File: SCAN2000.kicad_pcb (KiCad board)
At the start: 2 copper layers, 228.6 x 70.6 mm, 132 parts, among them J1 Conn_02x16_Row_Letter_First, J2 Conn_01x05, J3 Conn_01x02, J4 Screw_Terminal_01x02, J5 Screw_Terminal_01x10, J6 Screw_Terminal_01x10, J7 Screw_Terminal_01x02, J8 Screw_Terminal_01x10, J9 Screw_Terminal_01x10, U1 TPS73233DBVR, U10 TLP3558A, U11 TLP3558A, U12 TLP3558A, U13 TLP3558A, U14 TLP3558A, U15 TLP3558A, U16 TLP3558A, U17 TLP3558A, U18 TLP3558A, U19 TLP3558A, U20 TLP3558A, U21 TLP3558A, U22 TLP3558A, U23 TLP3558A, U24 TLP3558A, U25 TLP3558A, U26 TLP3558A, U27 TLP3558A, U28 TLP3558A, U29 TLP3558A, U3 STM32G070KBT6, U30 TLP3558A, U31 TLP3558A, U32 TLP3558A, U33 TLP3558A, U34 TLP3558A, U35 TLP3558A, U36 TLP3558A, U37 TLP3558A, U38 TLP3558A, U39 TLP3558A, U4 TLP3558A, U40 TLP3558A, U41 TLP3558A, U42 TLP3558A, U43 TLP3558A, U44 TLP3558A, U45 TLP3558A, U46 TLP3558A, U47 TLP3558A, U5 TLP3558A, U6 TLP3558A, U7 TLP3558A, U8 TLP3558A, U9 TLP3558A

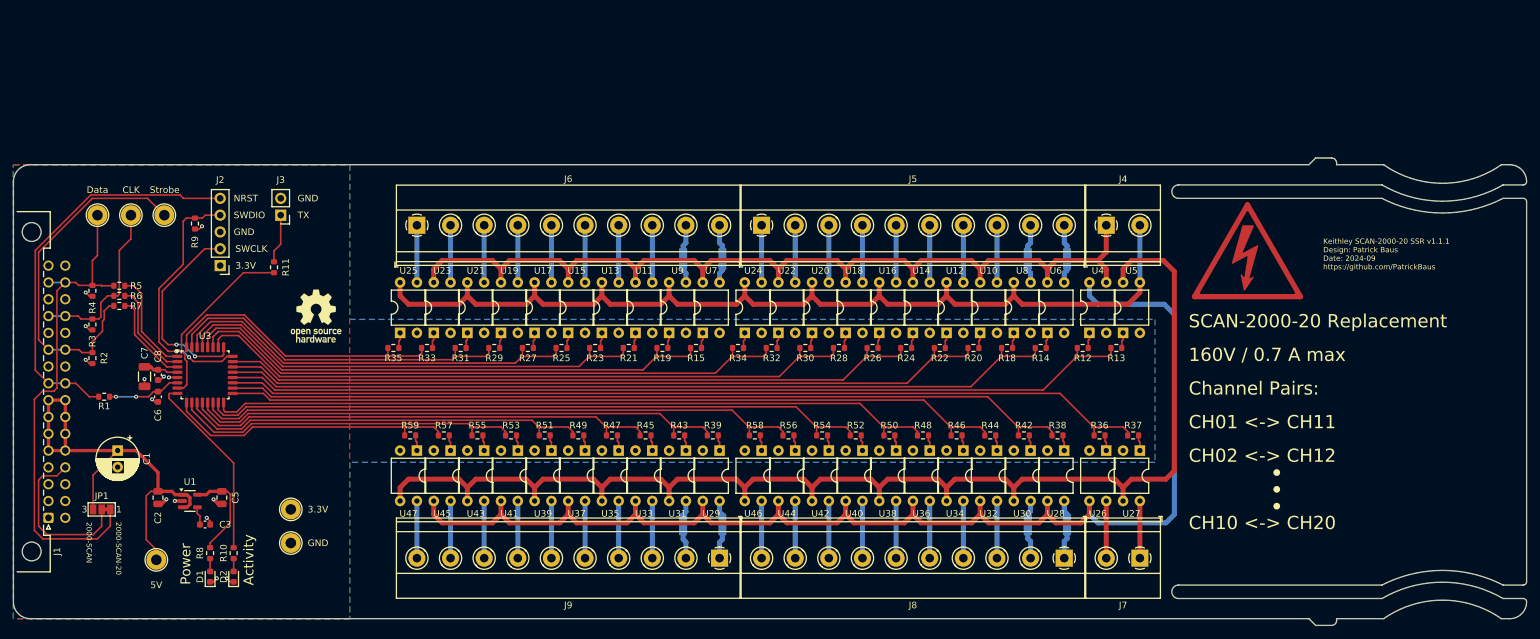
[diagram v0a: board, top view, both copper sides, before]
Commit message: Replaced the STM32 microcontroller with an iCE40 FPGA
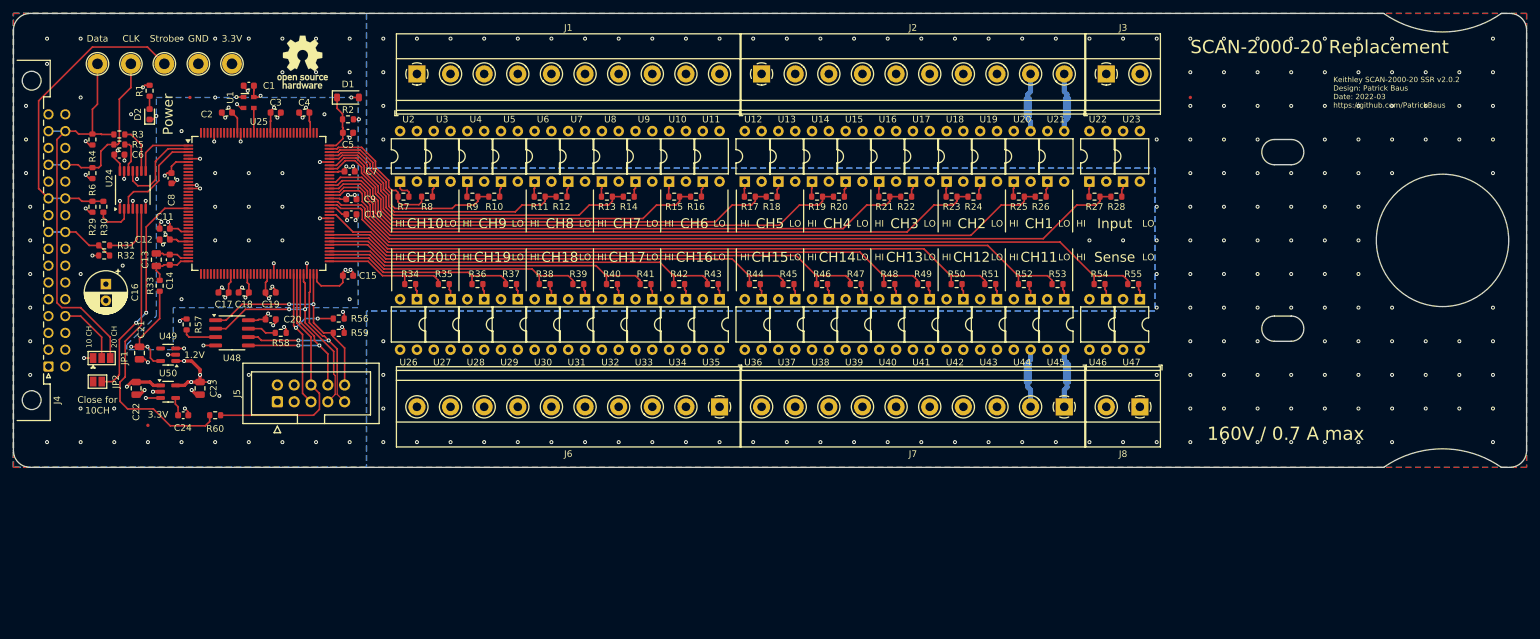
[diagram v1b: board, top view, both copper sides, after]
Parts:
- removed the D2 at (58.7, 110.5)
- removed the J2 at (56.6, 63.5)
- removed the J3 at (65.8, 55.9)
- removed the R10 at (58.7, 106.9)
- removed the R11 at (64.8, 63.8)
- removed the R17 at (129.5, 62.5)
- removed the R41 at (129.5, 102.6)
- removed the R9 at (52.8, 57.1)
- removed SYM1: SYM_Flash_Small, Symbol:Symbol_HighVoltage_Triangle_17x15mm_Copper
- removed the TP1 at (47.0, 108.0)
- removed the U3 at (54.4, 80.0)
- added C1: 100n, Capacitor_SMD:C_0603_1608Metric, F.Cu at (61.0, 36.3)
- added C10: 100n, Capacitor_SMD:C_0603_1608Metric, F.Cu at (76.5, 55.8)
- added C11: 100n, Capacitor_SMD:C_0603_1608Metric, F.Cu at (48.3, 57.9)
- added C12: 100n, Capacitor_SMD:C_0603_1608Metric, F.Cu at (48.3, 59.6)
- added C13: 10u, Capacitor_SMD:C_0805_2012Metric, F.Cu at (47.0, 62.6)
- added C14: 100n, Capacitor_SMD:C_0603_1608Metric, F.Cu at (49.0, 62.6)
- added C17: 100n, Capacitor_SMD:C_0603_1608Metric, F.Cu at (57.1, 67.6)
- added C18: 100n, Capacitor_SMD:C_0603_1608Metric, F.Cu at (60.2, 67.6)
- added C19: 100n, Capacitor_SMD:C_0603_1608Metric, F.Cu at (64.3, 67.6)
- added C2: 100n, Capacitor_SMD:C_0603_1608Metric, F.Cu at (57.7, 40.4)
- added C20: 100n, Capacitor_SMD:C_0603_1608Metric, F.Cu at (64.3, 71.6)
- added C21: 1u, Capacitor_SMD:C_0805_2012Metric, F.Cu at (44.5, 76.7)
- added C3: 100n, Capacitor_SMD:C_0603_1608Metric, F.Cu at (65.0, 40.4)
- added C4: 100n, Capacitor_SMD:C_0603_1608Metric, F.Cu at (69.3, 40.4)
- added C5: 100n, Capacitor_SMD:C_0603_1608Metric, F.Cu at (75.9, 43.4)
- added C8: 100n, Capacitor_SMD:C_0603_1608Metric, F.Cu at (49.3, 50.3)
- added C9: 100n, Capacitor_SMD:C_0603_1608Metric, F.Cu at (76.5, 53.5)
- added D1: 1N4448WQ-7-F, Diode_SMD:D_SOD-123, F.Cu at (75.9, 38.1)
- added FID1: Fiducial, Fiducial:Fiducial_0.5mm_Mask1mm, F.Cu at (52.1, 38.1)
- added FID2: Fiducial, Fiducial:Fiducial_0.5mm_Mask1mm, F.Cu at (203.2, 38.1)
- added FID3: Fiducial, Fiducial:Fiducial_0.5mm_Mask1mm, F.Cu at (45.7, 87.6)
- added J5: Conn_02x05_Odd_Even, Connector_IDC:IDC-Header_2x05_P2.54mm_Vertical, F.Cu at (65.3, 84.1)
- added JP2: SolderJumper_2_Open, Jumper:SolderJumper-2_P1.3mm_Open_Pad1.0x1.5mm, F.Cu at (38.1, 81.0)
- added R2: 33k, Resistor_SMD:R_0603_1608Metric, F.Cu at (75.9, 41.4)
- added R32: 10k, Resistor_SMD:R_0603_1608Metric, F.Cu at (39.1, 62.0)
- added R33: 100R, Resistor_SMD:R_0603_1608Metric, F.Cu at (47.5, 66.5)
- added R56: 10k, Resistor_SMD:R_0603_1608Metric, F.Cu at (74.5, 71.5)
- added R57: 10k, Resistor_SMD:R_0603_1608Metric, F.Cu at (51.6, 72.4)
- added R58: 10k, Resistor_SMD:R_0603_1608Metric, F.Cu at (65.8, 73.7)
- added R59: 10k, Resistor_SMD:R_0603_1608Metric, F.Cu at (74.5, 73.7)
- added R60: 10k, Resistor_SMD:R_0603_1608Metric, F.Cu at (55.9, 86.1)
- added U1: ASDAIG-16.000MHZ-C-S-T, Oscillator:Oscillator_SMD_Abracon_ASDMB-4Pin_2.5x2.0mm, F.Cu at (60.9, 38.9)
- added U24: 74LVC125, Package_SO:TSSOP-14_4.4x5mm_P0.65mm, F.Cu at (43.4, 52.1)
- added U25: ICE40HX1K-TQ144, Package_QFP:TQFP-144_20x20mm_P0.5mm, F.Cu at (62.5, 54.1)
- added U48: W25Q16JVS, Package_SO:SOIC-8_3.9x4.9mm_P1.27mm, F.Cu at (58.4, 73.7)
- added U49: TLV71312PQDBVRQ1, Package_TO_SOT_SMD:SOT-23-5, F.Cu at (48.8, 77.0)
- C7: value 4.7u -> 100n; footprint Capacitor_SMD:C_1206_3216Metric -> Capacitor_SMD:C_0603_1608Metric
- JP1: value SolderJumper_3_Bridged12 -> SolderJumper_3_Open; footprint Jumper:SolderJumper-3_P1.3mm_Bridged12_Pad1.0x1.5mm_NumberLabels -> Jumper:SolderJumper-3_P1.3mm_Open_Pad1.0x1.5mm
- U50: renamed from U1; value TPS73233DBVR -> LDK130M33RY
- moved TP4 73.7 mm to (53.3, 33.0)
- moved D2 70.4 mm to (46.0, 40.6)
- moved R1 70.4 mm to (46.0, 37.1)
- moved TP5 67.9 mm to (58.4, 33.0)
- moved C7 43.8 mm to (76.2, 49.3), turned to 0 degrees
- moved LOGO1 38.4 mm to (69.1, 32.8)
- moved C6 37.0 mm to (41.4, 46.7), turned to 0 degrees
- moved C15 32.4 mm to (75.9, 65.0), turned to 0 degrees
- moved C16 25.2 mm to (39.4, 66.3)
- moved R11 22.9 mm to (104.9, 53.1), turned to 0 degrees
- moved R19 22.9 mm to (146.8, 53.1), turned to 0 degrees
- moved R21 22.9 mm to (157.0, 53.1), turned to 0 degrees
- moved R27 22.9 mm to (188.7, 53.1), turned to 0 degrees
- moved R9 22.9 mm to (94.7, 53.1), turned to 0 degrees
- moved R13 22.9 mm to (115.1, 53.1), turned to 0 degrees
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- renumbered C8 to C15, C1 to C16, C2 to C22, C5 to C23, C3 to C24, D1 to D2, J6 to J1, J5 to J2, J4 to J3, J1 to J4, J9 to J6, J8 to J7, J7 to J8, LOGO2 to LOGO1, R8 to R1, R29 to R10, R27 to R11, R25 to R12, R23 to R13, R21 to R14, R19 to R15, R15 to R16, R34 to R17, R32 to R18, R30 to R19, R28 to R20, R26 to R21, R24 to R22, R22 to R23, R20 to R24, R18 to R25, R14 to R26, R12 to R27, R13 to R28, R2 to R29, R5 to R3, R7 to R30, R1 to R31, R59 to R34, R57 to R35, R55 to R36, R53 to R37, R51 to R38, R49 to R39, R47 to R40, R45 to R41, R43 to R42, R39 to R43, R58 to R44, R56 to R45, R54 to R46, R52 to R47, R50 to R48, R48 to R49, R6 to R5, R46 to R50, R44 to R51, R42 to R52, R38 to R53, R36 to R54, R37 to R55, R3 to R6, R16 to R61, R40 to R62, R35 to R7, R33 to R8, R31 to R9, TP4 to TP1, TP5 to TP2, TP6 to TP3, TP3 to TP4, TP2 to TP5, U9 to U10, U7 to U11, U24 to U12, U22 to U13, U20 to U14, U18 to U15, U14 to U17, U12 to U18, U10 to U19, U25 to U2, U8 to U20, U6 to U21, U4 to U22, U5 to U23, U47 to U26, U45 to U27, U43 to U28, U41 to U29, U23 to U3, U39 to U30, U37 to U31, U35 to U32, U31 to U34, U29 to U35, U46 to U36, U44 to U37, U42 to U38, U40 to U39, U21 to U4, U38 to U40, U36 to U41, U34 to U42, U32 to U43, U30 to U44, U28 to U45, U26 to U46, U27 to U47, U19 to U5, U17 to U6, U15 to U7, U13 to U8, U11 to U9
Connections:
- net /Microcontroller/Bus2_input_enable renamed /FPGA/Bus2_input_enable
- net /Microcontroller/Bus2_sense_enable renamed /FPGA/Bus2_sense_enable
- net /Microcontroller/CH1 renamed /FPGA/CH1
- net /Microcontroller/CH10 renamed /FPGA/CH10
- net /Microcontroller/CH11 renamed /FPGA/CH11
- net /Microcontroller/CH12 renamed /FPGA/CH12
- net /Microcontroller/CH13 renamed /FPGA/CH13
- net /Microcontroller/CH14 renamed /FPGA/CH14
- net /Microcontroller/CH15 renamed /FPGA/CH15
- net /Microcontroller/CH16 renamed /FPGA/CH16
- net /Microcontroller/CH17 renamed /FPGA/CH17
- net /Microcontroller/CH18 renamed /FPGA/CH18
- net /Microcontroller/CH19 renamed /FPGA/CH19
- net /Microcontroller/CH2 renamed /FPGA/CH2
- net /Microcontroller/CH20 renamed /FPGA/CH20
- net /Microcontroller/CH3 renamed /FPGA/CH3
- net /Microcontroller/CH4 renamed /FPGA/CH4
- net /Microcontroller/CH5 renamed /FPGA/CH5
- net /Microcontroller/CH6 renamed /FPGA/CH6
- net /Microcontroller/CH7 renamed /FPGA/CH7
- net /Microcontroller/CH8 renamed /FPGA/CH8
- net /Microcontroller/CH9 renamed /FPGA/CH9
- net Net-(J5-Pin_1) renamed /Relays/Input pins/IN.HI5
- net Net-(J5-Pin_10) renamed /Relays/Input pins/IN.LO1
- net Net-(J5-Pin_2) renamed /Relays/Input pins/IN.LO5
- net Net-(J5-Pin_3) renamed /Relays/Input pins/IN.HI4
- net Net-(J5-Pin_4) renamed /Relays/Input pins/IN.LO4
- net Net-(J5-Pin_5) renamed /Relays/Input pins/IN.HI3
- net Net-(J5-Pin_6) renamed /Relays/Input pins/IN.LO3
- net Net-(J5-Pin_7) renamed /Relays/Input pins/IN.HI2
- net Net-(J5-Pin_8) renamed /Relays/Input pins/IN.LO2
- net Net-(J5-Pin_9) renamed /Relays/Input pins/IN.HI1
- net Net-(J6-Pin_1) renamed /Relays/Input pins/IN.HI10
- net Net-(J6-Pin_10) renamed /Relays/Input pins/IN.LO6
- net Net-(J6-Pin_2) renamed /Relays/Input pins/IN.LO10
- net Net-(J6-Pin_3) renamed /Relays/Input pins/IN.HI9
- net Net-(J6-Pin_4) renamed /Relays/Input pins/IN.LO9
- net Net-(J6-Pin_5) renamed /Relays/Input pins/IN.HI8
- net Net-(J6-Pin_6) renamed /Relays/Input pins/IN.LO8
- net Net-(J6-Pin_7) renamed /Relays/Input pins/IN.HI7
- net Net-(J6-Pin_8) renamed /Relays/Input pins/IN.LO7
- net Net-(J6-Pin_9) renamed /Relays/Input pins/IN.HI6
- net Net-(J8-Pin_1) renamed /Relays/Input/Sense pins/IN.LO11
- net Net-(J8-Pin_10) renamed /Relays/Input/Sense pins/IN.HI15
- net Net-(J8-Pin_2) renamed /Relays/Input/Sense pins/IN.HI11
- net Net-(J8-Pin_3) renamed /Relays/Input/Sense pins/IN.LO12
- net Net-(J8-Pin_4) renamed /Relays/Input/Sense pins/IN.HI12
- net Net-(J8-Pin_5) renamed /Relays/Input/Sense pins/IN.LO13
- net Net-(J8-Pin_6) renamed /Relays/Input/Sense pins/IN.HI13
- net Net-(J8-Pin_7) renamed /Relays/Input/Sense pins/IN.LO14
- net Net-(J8-Pin_8) renamed /Relays/Input/Sense pins/IN.HI14
- net Net-(J8-Pin_9) renamed /Relays/Input/Sense pins/IN.LO15
- net Net-(J9-Pin_1) renamed /Relays/Input/Sense pins/IN.LO16
- net Net-(J9-Pin_10) renamed /Relays/Input/Sense pins/IN.HI20
- net Net-(J9-Pin_2) renamed /Relays/Input/Sense pins/IN.HI16
- net Net-(J9-Pin_3) renamed /Relays/Input/Sense pins/IN.LO17
- net Net-(J9-Pin_4) renamed /Relays/Input/Sense pins/IN.HI17
- net Net-(J9-Pin_5) renamed /Relays/Input/Sense pins/IN.LO18
- net Net-(J9-Pin_6) renamed /Relays/Input/Sense pins/IN.HI18
- net Net-(J9-Pin_7) renamed /Relays/Input/Sense pins/IN.LO19
- net Net-(J9-Pin_8) renamed /Relays/Input/Sense pins/IN.HI19
- net Net-(J9-Pin_9) renamed /Relays/Input/Sense pins/IN.LO20
- C6 pad 1: Net-(U3-NRST) -> +3V3
- J3 pad 1: /Relays/Input pins/Out_HIGH -> /Relays/Input pins/OUT.HI
- J3 pad 2: /Relays/Input pins/Out_LOW -> /Relays/Input pins/OUT.LO
- JP1 pad 1: /DATA -> +5V
- JP1 pad 3: +5V -> /DATA
- R3 pad 1: /Microcontroller/DATA -> Net-(R3-Pad1)
- R30 pad 1: /Microcontroller/STROBE -> Net-(R30-Pad1)
- R31 pad 1: Net-(U3-NRST) -> Net-(R31-Pad1)
- R5 pad 1: /Microcontroller/CLK -> Net-(R5-Pad1)
- U10 pad 4: /Relays/Input pins/Out_LOW -> /Relays/Input pins/OUT.HI
- U11 pad 4: /Relays/Input pins/Out_HIGH -> /Relays/Input pins/OUT.LO
- U12 pad 4: /Relays/Input pins/Out_LOW -> /Relays/Input pins/OUT.HI
- U13 pad 4: /Relays/Input pins/Out_HIGH -> /Relays/Input pins/OUT.LO
- U14 pad 4: /Relays/Input pins/Out_LOW -> /Relays/Input pins/OUT.HI
- U15 pad 4: /Relays/Input pins/Out_HIGH -> /Relays/Input pins/OUT.LO
- U16 pad 4: /Relays/Input pins/Out_LOW -> /Relays/Input pins/OUT.HI
- U17 pad 4: /Relays/Input pins/Out_HIGH -> /Relays/Input pins/OUT.LO
- U18 pad 4: /Relays/Input pins/Out_LOW -> /Relays/Input pins/OUT.HI
- U19 pad 4: /Relays/Input pins/Out_HIGH -> /Relays/Input pins/OUT.LO
- U2 pad 4: /Relays/Input pins/Out_LOW -> /Relays/Input pins/OUT.HI
- U20 pad 4: /Relays/Input pins/Out_LOW -> /Relays/Input pins/OUT.HI
- U21 pad 4: /Relays/Input pins/Out_HIGH -> /Relays/Input pins/OUT.LO
- U22 pad 3: /Relays/Input pins/Out_HIGH -> /Relays/Input pins/OUT.HI
- U22 pad 4: /Relays/Input pins/Bus_HIGH -> /Relays/Input pins/BUS.HI
- U23 pad 3: /Relays/Input pins/Out_LOW -> /Relays/Input pins/OUT.LO
- U23 pad 4: /Relays/Input pins/Bus_LOW -> /Relays/Input pins/BUS.LO
- U26 pad 3: /Relays/Input pins/Bus_LOW -> /Relays/Input pins/BUS.HI
- U27 pad 3: /Relays/Input pins/Bus_HIGH -> /Relays/Input pins/BUS.LO
- U28 pad 3: /Relays/Input pins/Bus_LOW -> /Relays/Input pins/BUS.HI
- U29 pad 3: /Relays/Input pins/Bus_HIGH -> /Relays/Input pins/BUS.LO
- U3 pad 4: /Relays/Input pins/Out_HIGH -> /Relays/Input pins/OUT.LO
- U30 pad 3: /Relays/Input pins/Bus_LOW -> /Relays/Input pins/BUS.HI
- U31 pad 3: /Relays/Input pins/Bus_HIGH -> /Relays/Input pins/BUS.LO
- U32 pad 3: /Relays/Input pins/Bus_LOW -> /Relays/Input pins/BUS.HI
- U33 pad 3: /Relays/Input pins/Bus_HIGH -> /Relays/Input pins/BUS.LO
- U34 pad 3: /Relays/Input pins/Bus_LOW -> /Relays/Input pins/BUS.HI
- U35 pad 3: /Relays/Input pins/Bus_HIGH -> /Relays/Input pins/BUS.LO
- U36 pad 3: /Relays/Input pins/Bus_LOW -> /Relays/Input pins/BUS.HI
- U37 pad 3: /Relays/Input pins/Bus_HIGH -> /Relays/Input pins/BUS.LO
- U38 pad 3: /Relays/Input pins/Bus_LOW -> /Relays/Input pins/BUS.HI
- U39 pad 3: /Relays/Input pins/Bus_HIGH -> /Relays/Input pins/BUS.LO
- U4 pad 4: /Relays/Input pins/Out_LOW -> /Relays/Input pins/OUT.HI
- U40 pad 3: /Relays/Input pins/Bus_LOW -> /Relays/Input pins/BUS.HI
- U41 pad 3: /Relays/Input pins/Bus_HIGH -> /Relays/Input pins/BUS.LO
- U42 pad 3: /Relays/Input pins/Bus_LOW -> /Relays/Input pins/BUS.HI
- U43 pad 3: /Relays/Input pins/Bus_HIGH -> /Relays/Input pins/BUS.LO
- U44 pad 3: /Relays/Input pins/Bus_LOW -> /Relays/Input pins/BUS.HI
- U45 pad 3: /Relays/Input pins/Bus_HIGH -> /Relays/Input pins/BUS.LO
- U46 pad 3: /Relays/Input pins/Bus_HIGH -> /Relays/Input pins/BUS.HI
- U47 pad 3: /Relays/Input pins/Bus_LOW -> /Relays/Input pins/BUS.LO
- U5 pad 4: /Relays/Input pins/Out_HIGH -> /Relays/Input pins/OUT.LO
- U6 pad 4: /Relays/Input pins/Out_LOW -> /Relays/Input pins/OUT.HI
- U7 pad 4: /Relays/Input pins/Out_HIGH -> /Relays/Input pins/OUT.LO
- U8 pad 4: /Relays/Input pins/Out_LOW -> /Relays/Input pins/OUT.HI
- U9 pad 4: /Relays/Input pins/Out_HIGH -> /Relays/Input pins/OUT.LO
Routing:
- net /Relays/Input pins/Bus_HIGH: track 194.1 -> 0.00 mm
- net /Relays/Input pins/Bus_LOW: track 192.0 -> 0.00 mm
- net /Relays/Input pins/BUS.HI: track 0.00 -> 190.5 mm
- net /Relays/Input pins/BUS.LO: track 0.00 -> 188.9 mm
- net /Relays/Input pins/Out_LOW: track 153.0 -> 0.00 mm
- net /Relays/Input pins/OUT.LO: track 0.00 -> 148.2 mm
- net /Relays/Input pins/OUT.HI: track 0.00 -> 145.4 mm
- net /Relays/Input pins/Out_HIGH: track 140.3 -> 0.00 mm
- net +5V: track 68.8 -> 10.2 mm, vias 0 -> 4
- net +3V3: track 20.0 -> 70.5 mm, vias 0 -> 24
- net /~{NRST}: track 61.0 -> 10.7 mm
- net Net-(R60-Pad1): track 0.00 -> 46.7 mm
- net /Microcontroller/SWDIO: track 38.4 -> 0.00 mm, vias 2 -> 0
- net /FPGA/~{CRESET}: track 0.00 -> 37.1 mm
- net /FPGA/SDI: track 0.00 -> 36.5 mm, vias 0 -> 2
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- added copper zone on B.Cu, net +1V2
- added copper zone on In2.Cu, net +3V3
- added copper zone on In2.Cu, net +5V
- added copper zone on F.Cu, net GND
- added copper zone on In1.Cu, net GND
- added copper zone on In2.Cu, net GND
- removed copper zone on F.Cu, net +3V3
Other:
- board size 228.6 x 70.6 mm -> 228.6 x 68.6 mm
- copper layers 2 -> 4
- board text added: "0.1855 mm"
- board text added: "0.2104 mm"
- board text added: "1.0300 mm"
- board text added: "1.0650 mm"
- board text added: "1.2V"
- board text added: "10 CH"
- board text added: "17 µm"
- board text added: "20 CH"
- board text added: "CH1"
- board text added: "CH10"
- board text added: "CH11"
- board text added: "CH12"
- board text added: "CH13"
- board text added: "CH14"
- board text added: "CH15"
- board text added: "CH16"
- board text added: "CH17"
- board text added: "CH18"
- board text added: "CH19"
- board text added: "CH2"
- board text added: "CH20"
- board text added: "CH3"
- board text added: "CH4"
- board text added: "CH5"
- board text added: "CH6"
- board text added: "CH7"
- board text added: "CH8"
- board text added: "CH9"
- board text added: "Close for 10CH"
- board text added: "Do not place any components above this line"
- board text added: "Do not place any components below this line"
- board text added: "HI"
- board text added: "Input"
- board text added: "Keithley SCAN-2000-20 SSR v2.0.2 Design: Patrick Baus Date: 2022-03 https://github.com/PatrickBaus"
- board text added: "LO"
- board text added: "Manufacturing Instruction: - Material FR-4 - Finished thickness: 1.57 mm ± 0.13 mm - Surface finish: ENIG - Solder mask color: Blue (preferred) or green (if the soldermask requires it) - Do not remove soldermask between the TQFP-144 pins - PCBs are to be RoHS compliant - Do not edit artwork, e.g. to add logos or order numbers - Clean to meet IPC J-STD-001E, Class 2 after assembly"
- board text added: "Prepreg 7628"
- board text added: "Sense"
- board text added: "Stackup: JLC04161H-7628"
- board text added: "Stackup: PCBWay"
- board text removed: "1.5 mm"
- board text removed: "2000-SCAN"
- board text removed: "2000-SCAN-20"
- board text removed: "5V"
- board text removed: "Activity"
- board text removed: "CH01 <-> CH11"
- board text removed: "CH02 <-> CH12"
- board text removed: "CH10 <-> CH20"
- board text removed: "Channel Pairs:"
- board text removed: "Keithley SCAN-2000-20 SSR v1.1.1 Design: Patrick Baus Date: 2024-09 https://github.com/PatrickBaus"
- board text removed: "Manufacturing Instruction: - Material FR-4 - Finished thickness: 1.57 mm ± 0.13 mm - Surface finish: ENIG - Solder mask color: Green - PCBs are to be RoHS compliant - Do not edit artwork, e.g. to add logos or order numbers - Clean to meet IPC J-STD-001E, Class 2 after assembly"
- board text removed: "NRST"
- board text removed: "No not place any components above this line"
- board text removed: "No not place any components below this line"
- board text removed: "SWCLK"
- board text removed: "SWDIO"
- board text removed: "Stackup:"
- board text removed: "TX"

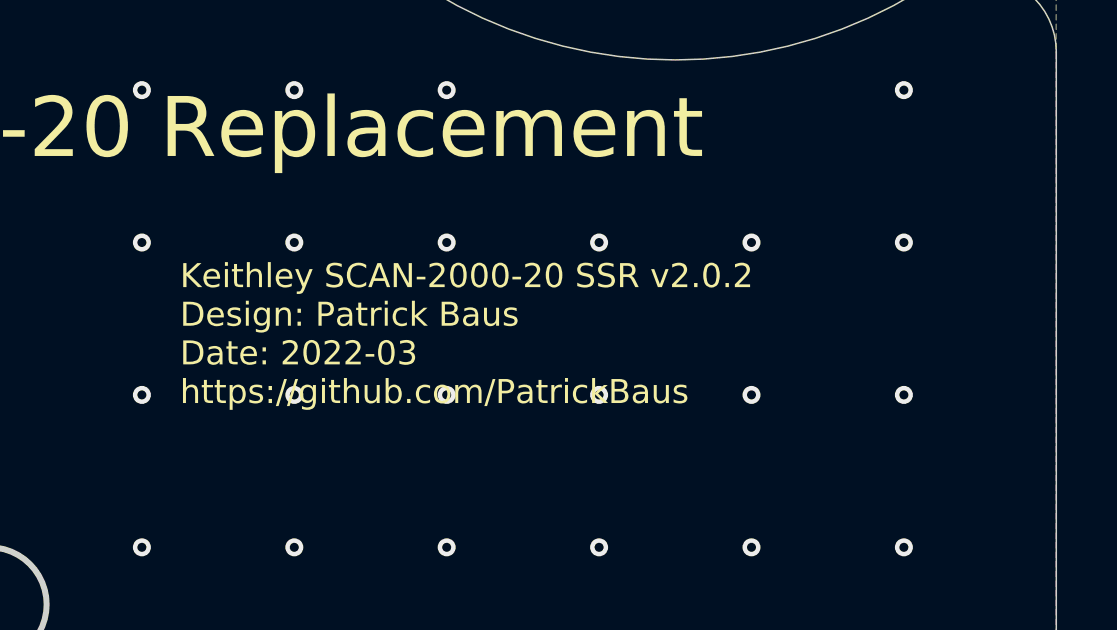
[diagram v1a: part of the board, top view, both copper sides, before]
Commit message: Bump version to 2.0.2, because of the update to KiCad 8
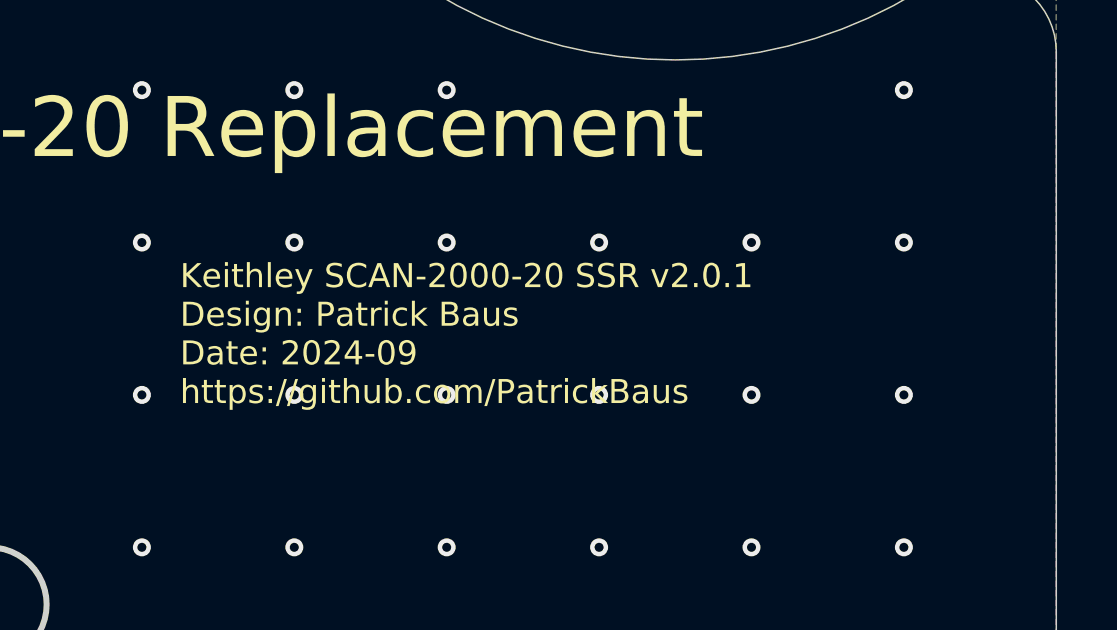
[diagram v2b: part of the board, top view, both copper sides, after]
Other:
- board text added: "Keithley SCAN-2000-20 SSR v2.0.1 Design: Patrick Baus Date: 2024-09 https://github.com/PatrickBaus"
- board text removed: "Keithley SCAN-2000-20 SSR v2.0.2 Design: Patrick Baus Date: 2022-03 https://github.com/PatrickBaus"
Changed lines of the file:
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@@
 		(layer "Edge.Cuts")
 	)
-	(gr_text "Keithley SCAN-2000-20 SSR v2.0.2\nDesign: Patrick Baus\nDate: 2022-03\nhttps://github.com/PatrickBaus"
+	(gr_text "Keithley SCAN-2000-20 SSR v2.0.1\nDesign: Patrick Baus\nDate: 2024-09\nhttps://github.com/PatrickBaus"
 		(at 224.79 37.338 0)
 		(layer "F.SilkS")

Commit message: Bump PCB version to 2.0.2
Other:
- board text added: "Keithley SCAN-2000-20 SSR v2.0.2 Design: Patrick Baus Date: 2024-09 https://github.com/PatrickBaus"
- board text removed: "Keithley SCAN-2000-20 SSR v2.0.1 Design: Patrick Baus Date: 2024-09 https://github.com/PatrickBaus"
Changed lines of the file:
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@@
 		(title "Keithley SCAN-2000-20 SSR")
 		(date "2024-09-26")
-		(rev "2.0.1")
+		(rev "2.0.2")
 		(comment 1 "Copyright (©) 2024, Patrick Baus <patrick.baus@physik.tu-darmstadt.de>")
 		(comment 2 "Licensed under CERN-OHL-W")
@@
 		(layer "Edge.Cuts")
 	)
-	(gr_text "Keithley SCAN-2000-20 SSR v2.0.1\nDesign: Patrick Baus\nDate: 2024-09\nhttps://github.com/PatrickBaus"
+	(gr_text "Keithley SCAN-2000-20 SSR v2.0.2\nDesign: Patrick Baus\nDate: 2024-09\nhttps://github.com/PatrickBaus"
 		(at 224.79 37.338 0)
 		(layer "F.SilkS")
